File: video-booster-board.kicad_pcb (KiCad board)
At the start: 4 copper layers, 36.5 x 41.5 mm, 133 parts, among them IC1 INA180A1IDBVT, J1 0473460001, J10 M20-9990246, J11 MC-HVT1-S04-G, J2 HDMI-PE10-19-LF, J3 HDMI-PE10-19-LF, J6 685119134923_, J9 685119134923_, SW1 1571983-5, U1 PTN3363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

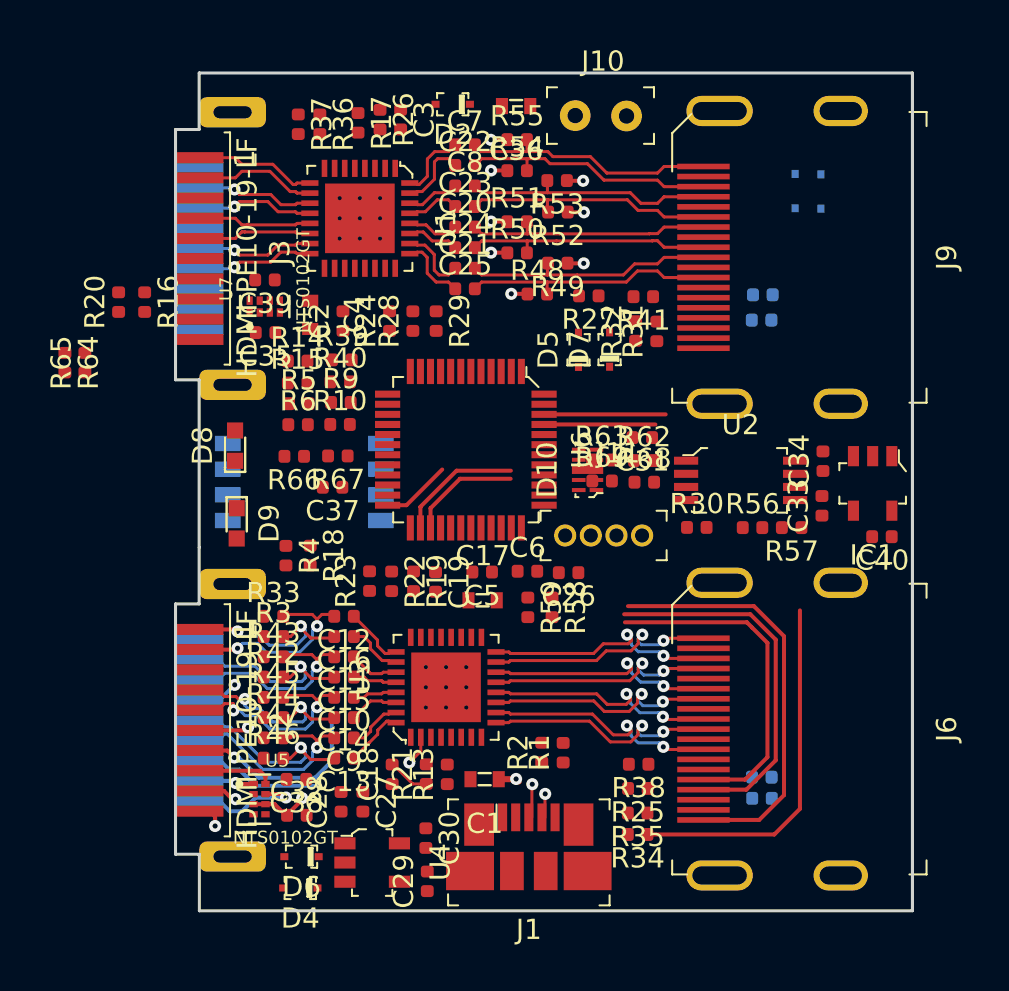
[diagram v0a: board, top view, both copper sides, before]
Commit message: PCB routing: HDMI,control, USB
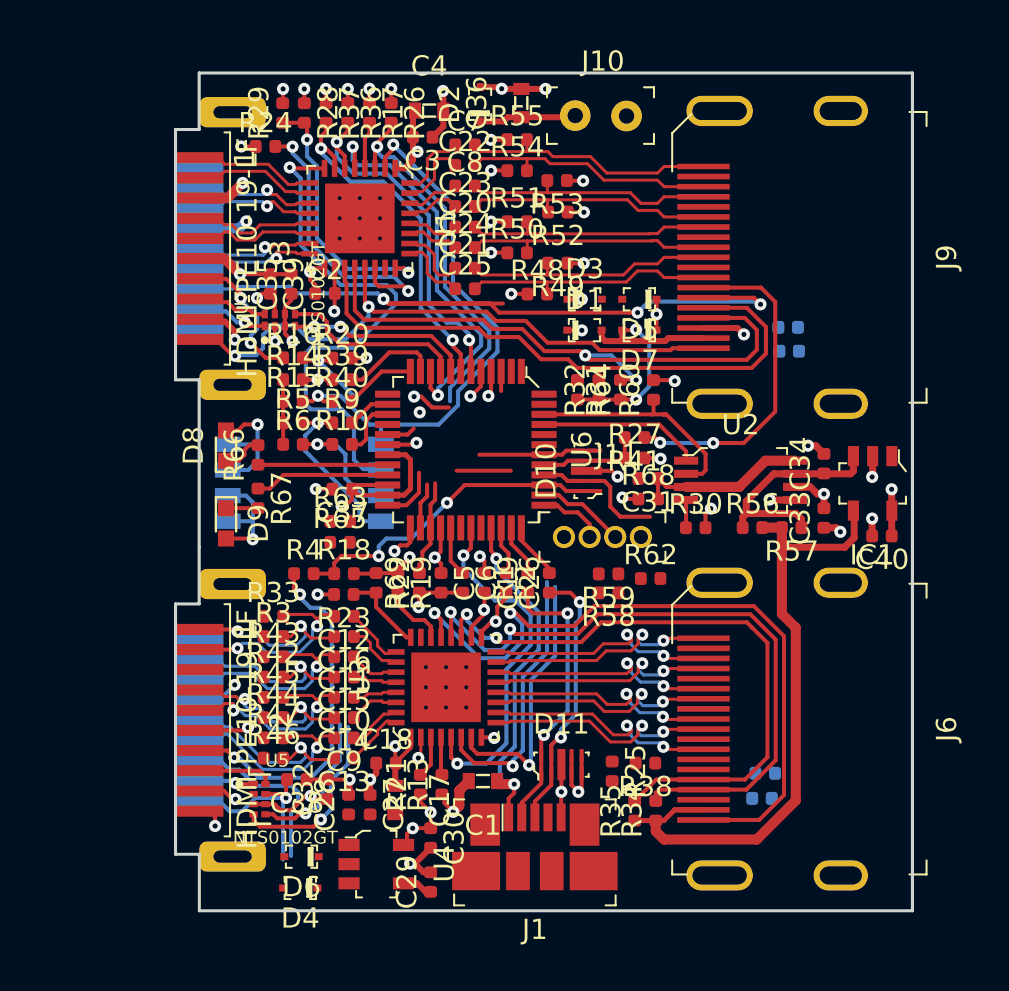
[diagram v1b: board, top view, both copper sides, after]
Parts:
- added D11: RCLAMP0524PATCT_, video-booster-board-footprints:UFDFN-10_2.5x1mm, F.Cu at (132.6, 92.8)
- added R60: R_100k_0402, video-booster-board-footprints:0402-res, F.Cu at (137.2, 74.2)
- D1, D3: moved to F.Cu
- D10: value RCLAMP0524PATCT -> RCLAMP0524PATCT_
- moved R64 25.4 mm to (133.4, 74.2)
- moved R65 15.5 mm to (121.6, 81.8), turned to 0 degrees
- moved R63 13.3 mm to (121.7, 80.7)
- moved D3 12.9 mm to (133.8, 69.7), turned to 0 degrees
- moved R29 12.8 mm to (118.8, 60.5), turned to 90 degrees
- moved D1 12.5 mm to (133.8, 71.2), turned to 0 degrees
- moved C4 11.7 mm to (126.1, 60.4), turned to 0 degrees
- moved R28 11.6 mm to (119.9, 60.5), turned to 270 degrees
- moved R20 11.4 mm to (121.8, 72.6), turned to 0 degrees
- moved C17 10.8 mm to (124.4, 94.5), turned to 270 degrees
- moved R24 10.6 mm to (118.0, 62.1), turned to 0 degrees
- moved R69 10.4 mm to (125.6, 83.8), turned to 90 degrees
- moved R1 8.59 mm to (130.9, 83.8)
- moved R2 8.41 mm to (132.0, 83.8)
- moved R27 8.35 mm to (136.2, 77.6), turned to 0 degrees
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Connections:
- net Net-(J1-Pad2) renamed /UDN
- net Net-(J1-Pad3) renamed /UDP
- R66 pad 1: /DBG_LED_1 -> /DBG_LED_RX
- R67 pad 1: /DBG_LED_0 -> /DBG_LED_TX
- SW1 pad 1.1: /TX_EQ0 -> /RX_EQ1
- SW1 pad 2.1: /TX_EQ1 -> /RX_EQ0
- SW1 pad 3.1: /RX_EQ0 -> /TX_EQ1
- SW1 pad 4.1: /RX_EQ1 -> /TX_EQ0
- U6 pad 13: /TX_EQ0_R -> Net-(U6-Pad13)
- U6 pad 14: /TX_EQ1_R -> /TX_EQ0_R
- U6 pad 15: Net-(U6-Pad15) -> /TX_EQ1_R
- U6 pad 20: /DBG_LED_0 -> /DBG_LED_RX
- U6 pad 21: /DBG_LED_1 -> /DBG_LED_TX
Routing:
- net GND: track 7.40 -> 77.2 mm, vias 3 -> 37
- net +3V3: track 11.6 -> 55.8 mm, vias 9 -> 28
- net /RX_UTILITY: track 0.00 -> 37.3 mm, vias 0 -> 3
- net /RX_HPD: track 0.00 -> 31.3 mm, vias 0 -> 2
- net /RX_SRC_SDA: track 0.00 -> 30.9 mm, vias 0 -> 2
- net /RX_SRC_SCL: track 0.00 -> 29.9 mm
- net /RX_EQ0: track 0.00 -> 28.3 mm, vias 0 -> 2
- net /RX_EQ1: track 0.00 -> 27.7 mm, vias 0 -> 2
- net /VUSB: track 1.05 -> 21.4 mm, vias 1 -> 3
- net /RX_DDET: track 0.00 -> 20.1 mm, vias 0 -> 2
- net /RX_HPD_3V: track 0.00 -> 19.2 mm, vias 0 -> 2
- net /RX_SRC_SDA_3V: track 0.00 -> 18.0 mm, vias 0 -> 2
- net /RX_SRC_SCL_3V: track 0.00 -> 17.7 mm, vias 0 -> 2
- net /TX_HPD_3V: track 0.00 -> 17.6 mm, vias 0 -> 2
- net Net-(J9-Pad13): track 0.00 -> 16.5 mm, vias 0 -> 2
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- added copper zone on In2.Cu, net +3V3
- removed copper zone on In2.Cu, net +5V

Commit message: Routing completed. Minor changes in control pins placement
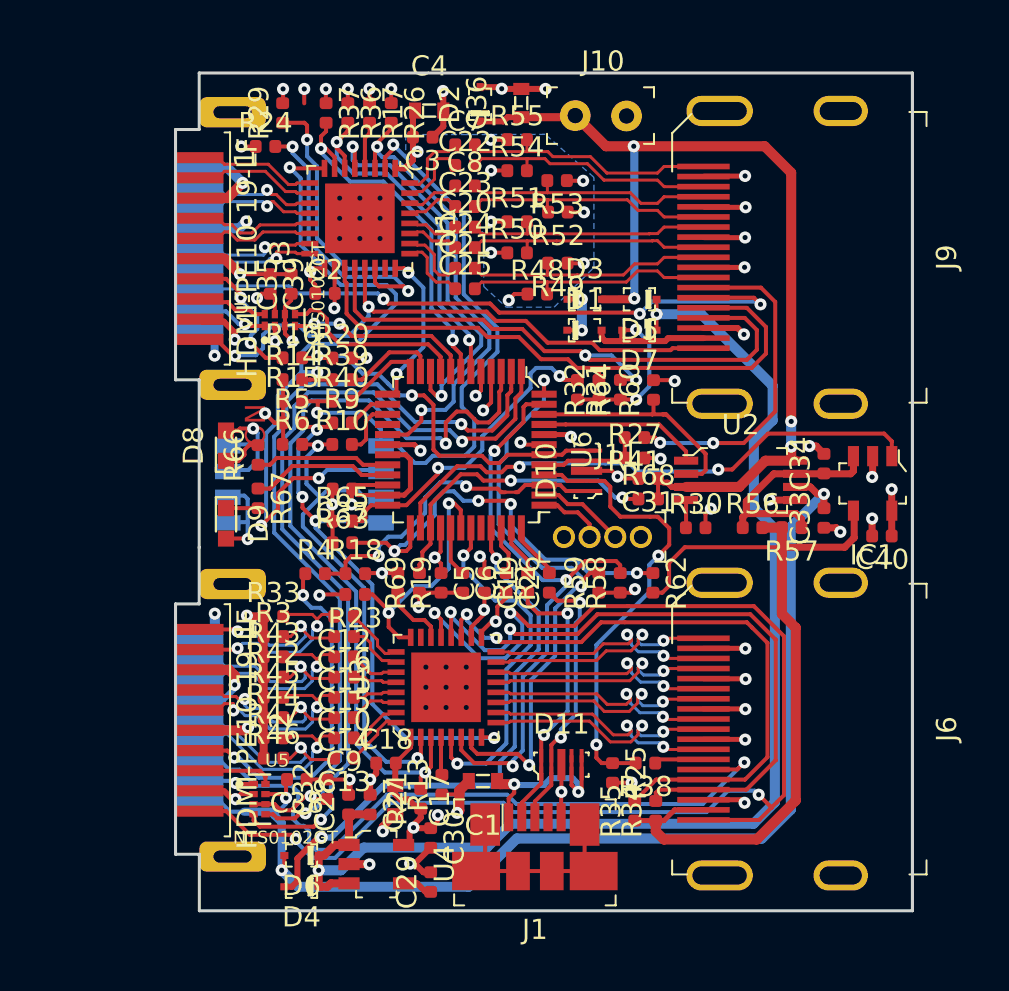
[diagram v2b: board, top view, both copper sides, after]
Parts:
- removed R11, R12, R7, R8: R_0R_0402, video-booster-board-footprints:0402-res
- removed R22, R28: R_10k_0402, video-booster-board-footprints:0402-res
- moved R63 1.07 mm to (121.8, 81.8)
- moved R65 1.06 mm to (121.8, 80.7)
- moved R58 0.76 mm to (135.5, 83.8), turned to 90 degrees
- moved R21 0.70 mm to (125.6, 94.5)
- moved R59 0.66 mm to (134.5, 83.8), turned to 90 degrees
- moved R18 0.56 mm to (122.4, 83.3)
- moved R23 0.56 mm to (122.4, 84.3)
- moved R4 0.56 mm to (120.4, 83.3)
- moved R62 0.24 mm to (137.1, 83.8), turned to 270 degrees
- moved D4 0.08 mm to (119.7, 98.8)
- moved R25 0.08 mm to (135.1, 93.2)
- moved SW1 0.08 mm to (119.9, 78.9)
- moved D6 0.06 mm to (119.7, 97.3)
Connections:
- IC1 pad 1: /ADC4 -> /ADC6
- R64 pad 1: /ADC6 -> /ADC4
- R65 pad 2: /ADC6 -> /ADC4
- U6 pad 13: Net-(U6-Pad13) -> /RX_HIZ_EN
- U6 pad 30: Net-(U6-Pad30) -> /TX_HIZ_EN
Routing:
- net +5V: track 1.53 -> 61.6 mm, vias 1 -> 2
- net /TX_SRC_5V: track 12.2 -> 56.7 mm, vias 2 -> 3
- net /TX_DDET: track 3.05 -> 39.5 mm, vias 0 -> 2
- net +5VA: track 13.3 -> 48.1 mm, vias 0 -> 4
- net GND: track 77.2 -> 110.3 mm, vias 37 -> 50
- net /TX_SRC_SDA_3V: track 9.06 -> 41.7 mm, vias 1 -> 2
- net /TX_SRC_SCL_3V: track 7.44 -> 39.8 mm, vias 1 -> 2
- net /TX_HPD: track 37.2 -> 67.8 mm, vias 3 -> 4
- net /TX_UTILITY: track 9.84 -> 35.6 mm, vias 0 -> 1
- net /ADC6: track 4.98 -> 27.5 mm, vias 0 -> 2
- net /ADC5: track 1.95 -> 21.1 mm, vias 1 -> 4
- net /TX_EQ0: track 9.28 -> 27.9 mm, vias 2 -> 4
- net /TX_EQ1: track 7.44 -> 26.0 mm
- net /VUSB: track 21.4 -> 39.6 mm, vias 3 -> 4
- net /TX_SINK_SDA_3V: track 13.3 -> 29.9 mm, vias 1 -> 3
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- added copper zone on B.Cu, net +3V3
- added copper zone on In2.Cu, net /RX_SINK_5V
- added copper zone on In2.Cu, net GND

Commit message: Design Rules errors resolved
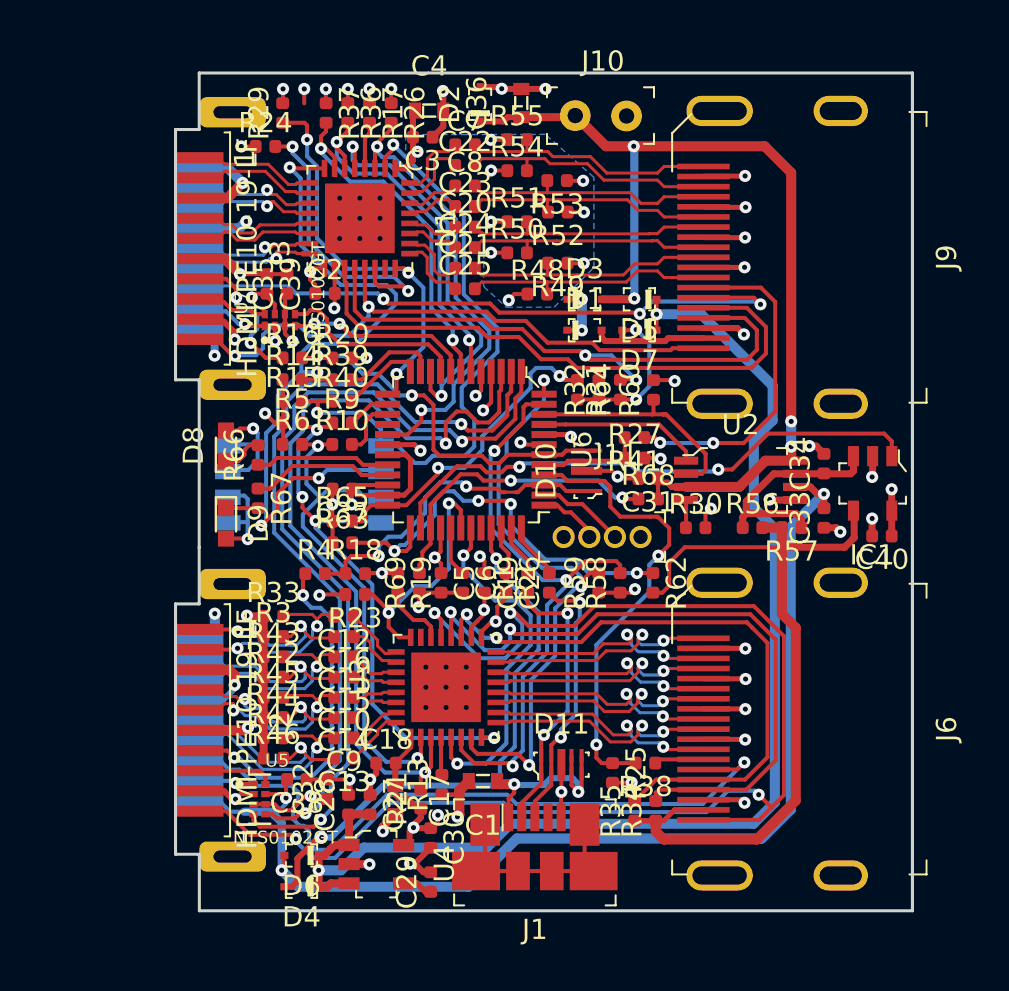
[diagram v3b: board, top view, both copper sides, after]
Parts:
- moved C35 0.20 mm to (119.0, 69.0)
- moved C39 0.16 mm to (118.0, 69.0)
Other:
- net class Default: clearance 0.2 -> 0.15
- rule trace_clearance: 0.2 -> 0.15

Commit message: Component designators arranged on PCB
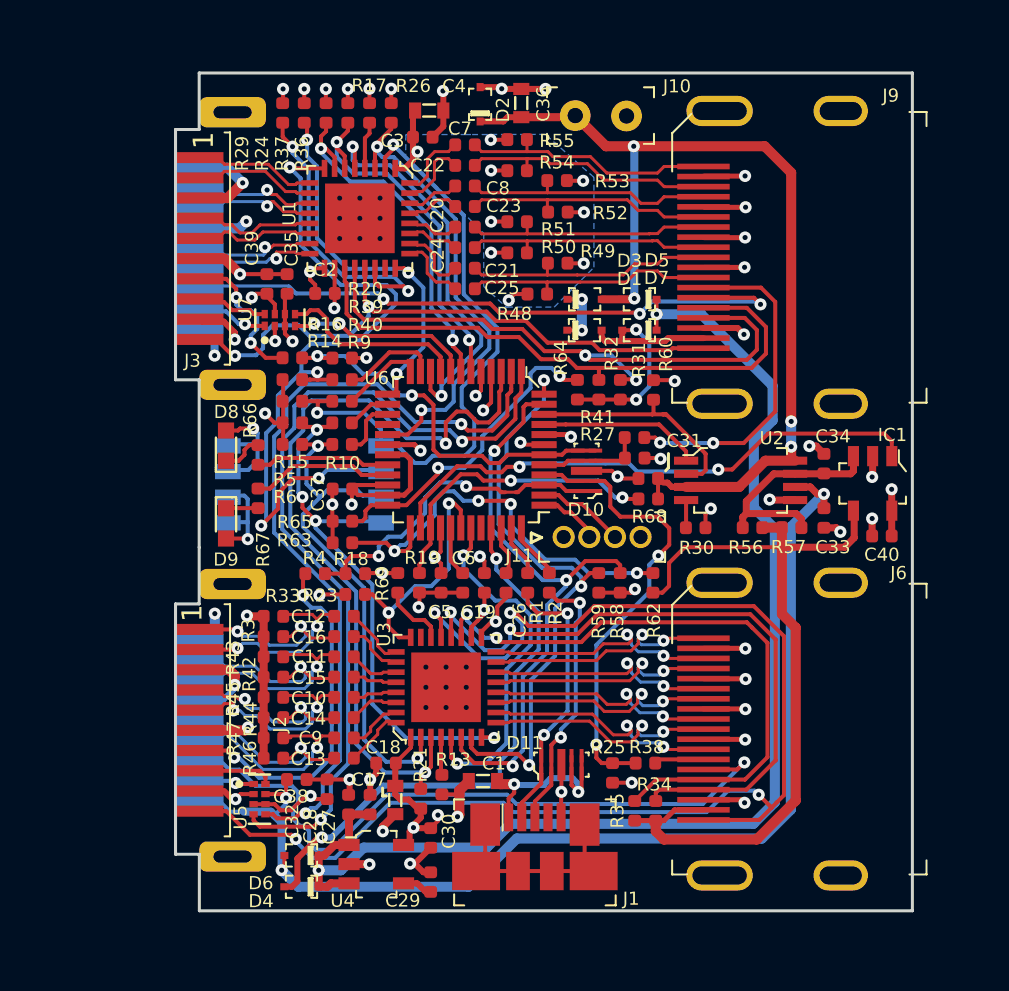
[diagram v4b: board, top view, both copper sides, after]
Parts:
- moved R24 1.86 mm to (118.8, 60.5), turned to 270 degrees
- moved R29 1.07 mm to (119.9, 60.5)
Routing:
- net /RX_HIZ_EN: track 20.3 -> 19.2 mm
- net +3V3: track 69.1 -> 68.4 mm, vias 32 -> 31
- net /RX_DCC_EN: track 14.4 -> 14.9 mm
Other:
- board text added: "Rx0"
- board text added: "Rx1"
- board text added: "Tx0"
- board text added: "Tx1"

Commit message: Differential lanes tuned
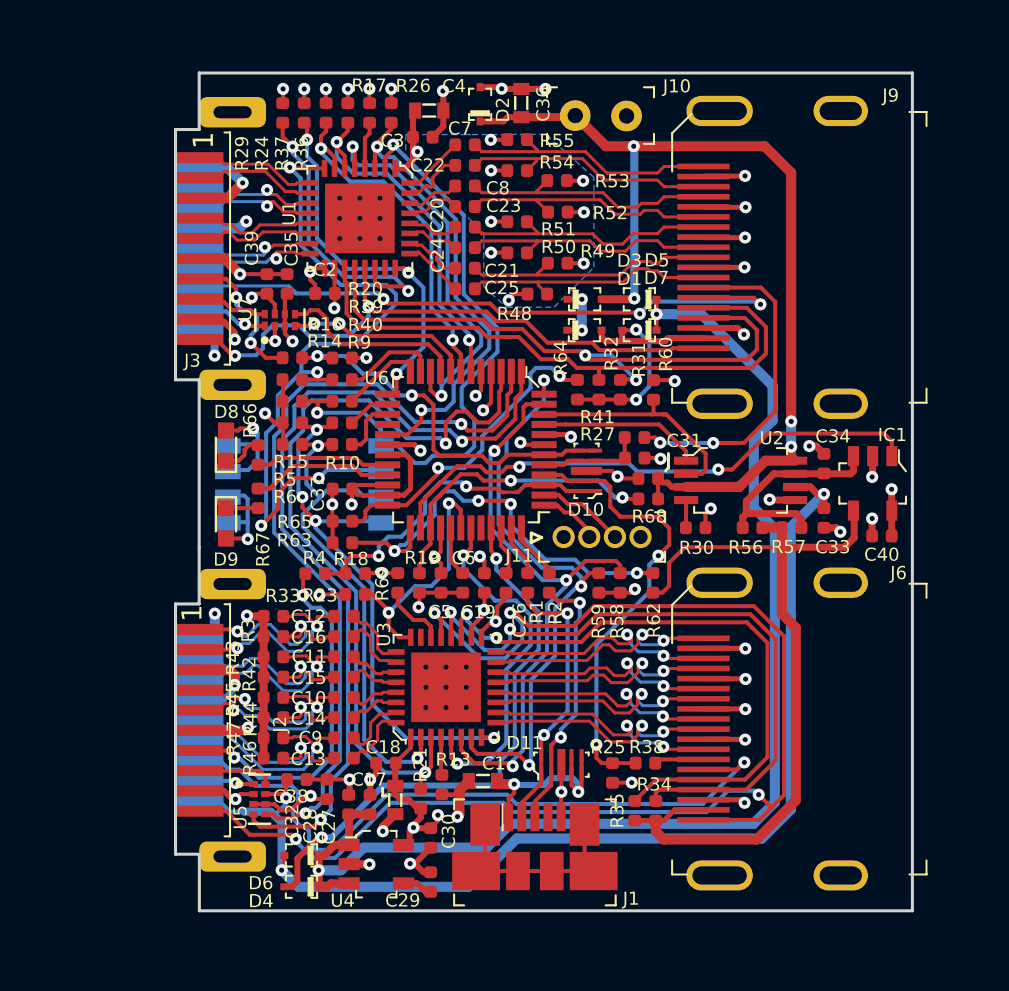
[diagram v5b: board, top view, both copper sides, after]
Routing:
- net /TX_IN_D2_P: track 9.44 -> 11.4 mm
- net /TX_IN_D1_P: track 9.43 -> 10.2 mm
- net /TX_IN_D1_N: track 10.1 -> 10.9 mm
- net /TX_IN_D2_N: track 10.1 -> 10.8 mm
- net /RX_IN_D0_P: track 12.2 -> 12.9 mm
- net /RX_IN_D0_N: track 12.2 -> 12.8 mm
- net /C_TX_IN_CLK_N: track 2.73 -> 3.30 mm
- net /C_TX_IN_D2_P: track 2.79 -> 3.30 mm

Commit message: Additional decoupling on MCU adn TX_SINK_5V added
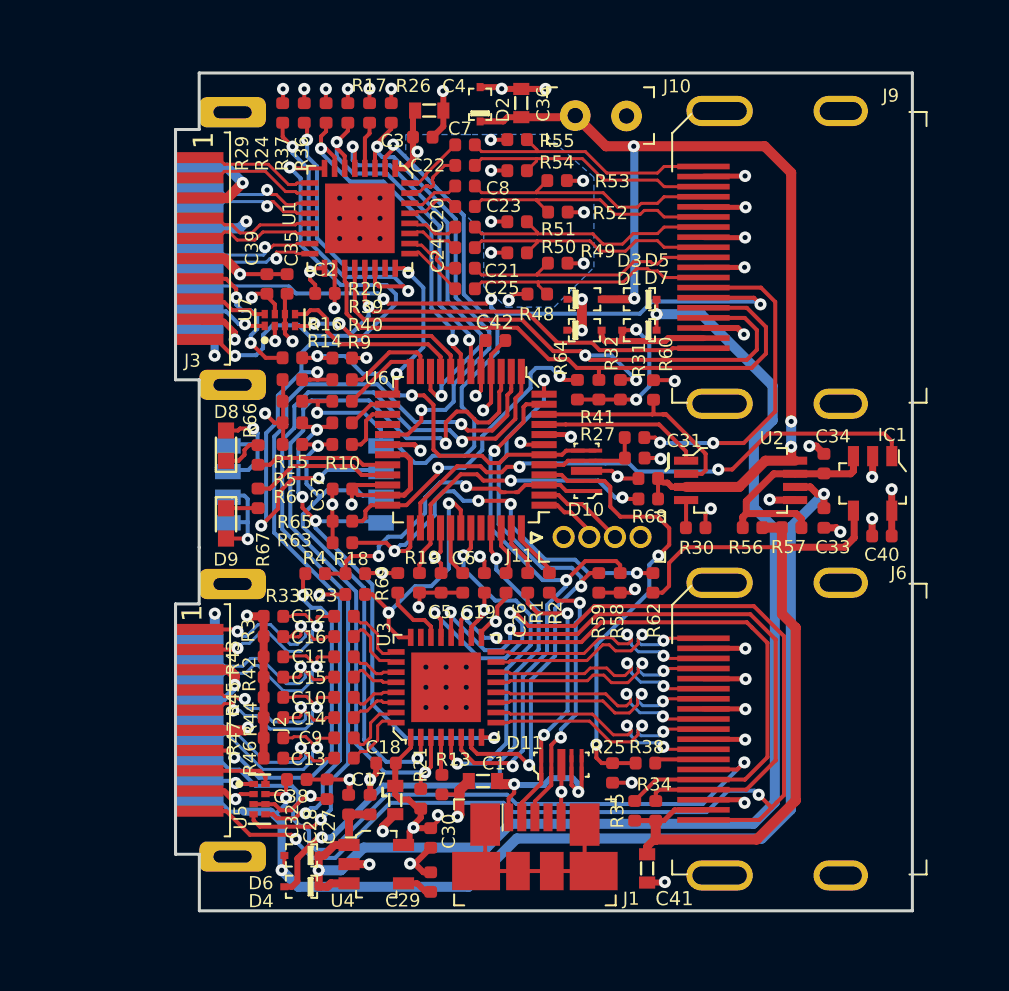
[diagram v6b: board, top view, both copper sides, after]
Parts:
- added C41: C_10u_0603, video-booster-board-footprints:0603-cap, F.Cu at (136.9, 97.9)
- added C42: C_1u_0402, video-booster-board-footprints:0402-cap, F.Cu at (129.3, 71.8)
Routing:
- net GND: track 110.3 -> 112.8 mm, vias 50 -> 51
- net +3V3: track 68.4 -> 70.2 mm
- net /TX_SINK_5V: track 40.0 -> 41.2 mm
